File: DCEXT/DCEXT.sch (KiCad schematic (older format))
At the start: 5 parts, among them U1 MPCIE-Socket

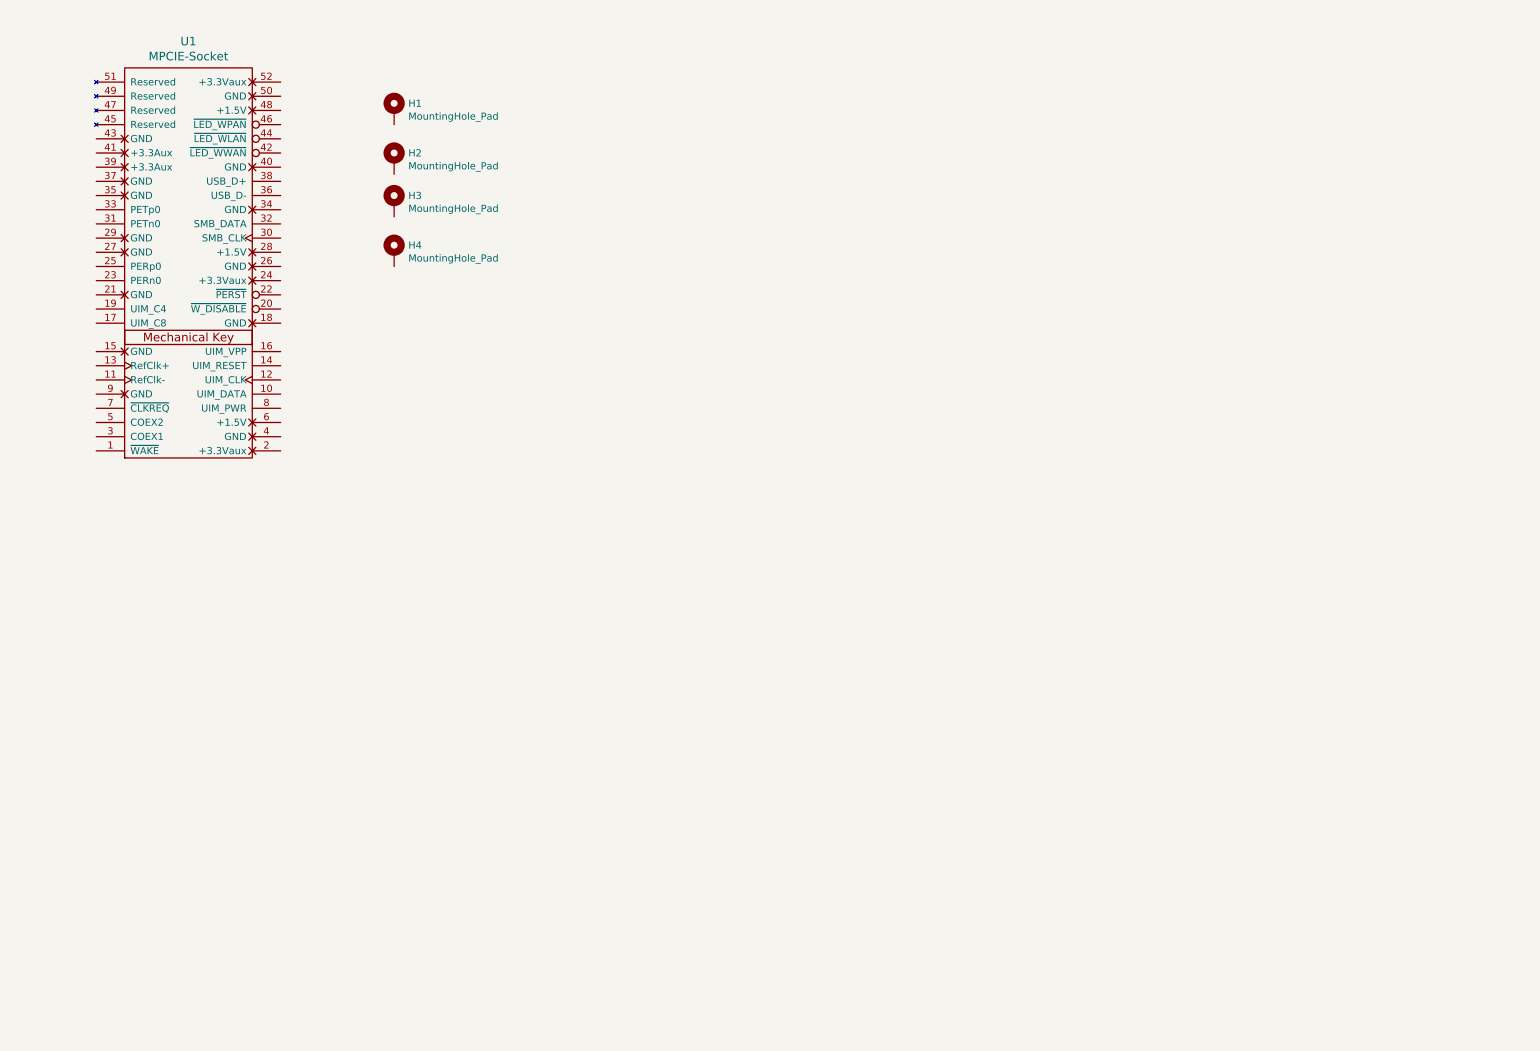
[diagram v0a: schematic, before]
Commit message: Add usb host connector and add more documentation
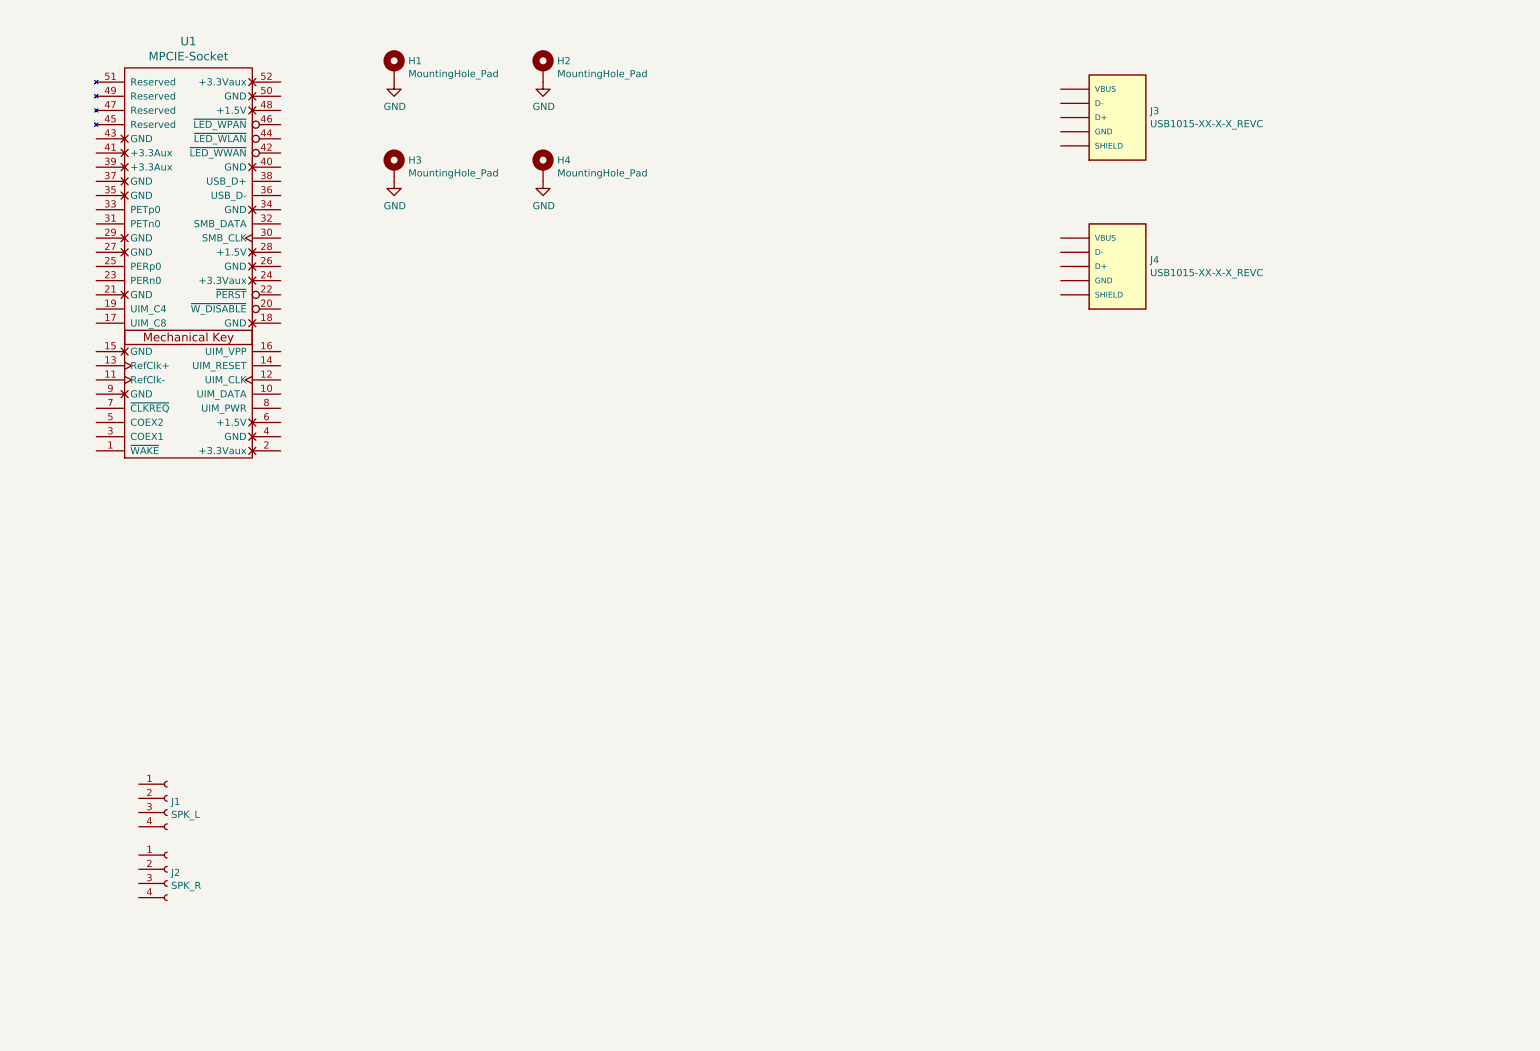
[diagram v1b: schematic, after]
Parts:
- added J1: SPK_L, symbol Connector:Conn_01x04_Female
- added J2: SPK_R, symbol Connector:Conn_01x04_Female
- added J3, J4: USB1015-XX-X-X_REVC, DCEXT:GCT_USB1015-XX-X-X_REVC, symbol USB1015-XX-X-X_REVC:USB1015-XX-X-X_REVC
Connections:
- net GND: now reaches H1.1
- net GND: now also H2.1, H3.1, H4.1
- new net: J3.5 (SHIELD), J3.6 (SHIELD), J3.7 (SHIELD), J3.8 (SHIELD)
- new net: J4.5 (SHIELD), J4.6 (SHIELD), J4.7 (SHIELD), J4.8 (SHIELD)
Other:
- moved on the sheet: H1, H2, H3, H4
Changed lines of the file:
@@
 L Mechanical:MountingHole_Pad H1
 U 1 1 613EA83B
-P 3200 1200
-F 0 "H1" H 3300 1249 50  0000 L CNN
-F 1 "MountingHole_Pad" H 3300 1158 50  0000 L CNN
-F 2 "MountingHole:MountingHole_5mm_Pad_TopBottom" H 3200 1200 50  0001 C CNN
-F 3 "~" H 3200 1200 50  0001 C CNN
-	1    3200 1200
+P 3200 900
+F 0 "H1" H 3300 949 50  0000 L CNN
+F 1 "MountingHole_Pad" H 3300 858 50  0000 L CNN
+F 2 "MountingHole:MountingHole_5mm_Pad_TopBottom" H 3200 900 50  0001 C CNN
+F 3 "~" H 3200 900 50  0001 C CNN
+	1    3200 900
 	1    0    0    -1
 $EndComp
@@
 L Mechanical:MountingHole_Pad H2
 U 1 1 613EB1E4
-P 3200 1550
-F 0 "H2" H 3300 1599 50  0000 L CNN
-F 1 "MountingHole_Pad" H 3300 1508 50  0000 L CNN
-F 2 "MountingHole:MountingHole_5mm_Pad_TopBottom" H 3200 1550 50  0001 C CNN
-F 3 "~" H 3200 1550 50  0001 C CNN
-	1    3200 1550
+P 4250 900
+F 0 "H2" H 4350 949 50  0000 L CNN
+F 1 "MountingHole_Pad" H 4350 858 50  0000 L CNN
+F 2 "MountingHole:MountingHole_5mm_Pad_TopBottom" H 4250 900 50  0001 C CNN
+F 3 "~" H 4250 900 50  0001 C CNN
+	1    4250 900
 	1    0    0    -1
 $EndComp
@@
 L Mechanical:MountingHole_Pad H3
 U 1 1 613EC01C
-P 3200 1850
-F 0 "H3" H 3300 1899 50  0000 L CNN
-F 1 "MountingHole_Pad" H 3300 1808 50  0000 L CNN
-F 2 "MountingHole:MountingHole_5mm_Pad_TopBottom" H 3200 1850 50  0001 C CNN
-F 3 "~" H 3200 1850 50  0001 C CNN
-	1    3200 1850
+P 3200 1600
+F 0 "H3" H 3300 1649 50  0000 L CNN
+F 1 "MountingHole_Pad" H 3300 1558 50  0000 L CNN
+F 2 "MountingHole:MountingHole_5mm_Pad_TopBottom" H 3200 1600 50  0001 C CNN
+F 3 "~" H 3200 1600 50  0001 C CNN
+	1    3200 1600
 	1    0    0    -1
 $EndComp
@@
 L Mechanical:MountingHole_Pad H4
 U 1 1 613EC022
-P 3200 2200
-F 0 "H4" H 3300 2249 50  0000 L CNN
-F 1 "MountingHole_Pad" H 3300 2158 50  0000 L CNN
-F 2 "MountingHole:MountingHole_5mm_Pad_TopBottom" H 3200 2200 50  0001 C CNN
-F 3 "~" H 3200 2200 50  0001 C CNN
-	1    3200 2200
+P 4250 1600
+F 0 "H4" H 4350 1649 50  0000 L CNN
+F 1 "MountingHole_Pad" H 4350 1558 50  0000 L CNN
+F 2 "MountingHole:MountingHole_5mm_Pad_TopBottom" H 4250 1600 50  0001 C CNN
+F 3 "~" H 4250 1600 50  0001 C CNN
+	1    4250 1600
 	1    0    0    -1
 $EndComp
+$Comp
+L power:GND #PWR0101
+U 1 1 613EFFE7
+P 3200 1000
+F 0 "#PWR0101" H 3200 750 50  0001 C CNN
+F 1 "GND" H 3205 827 50  0000 C CNN
+F 2 "" H 3200 1000 50  0001 C CNN
+F 3 "" H 3200 1000 50  0001 C CNN
+	1    3200 1000
+	1    0    0    -1
+$EndComp
+$Comp
+L power:GND #PWR0102
+U 1 1 613F3AAA
+P 4250 1000
+F 0 "#PWR0102" H 4250 750 50  0001 C CNN
+F 1 "GND" H 4255 827 50  0000 C CNN
+F 2 "" H 4250 1000 50  0001 C CNN
+F 3 "" H 4250 1000 50  0001 C CNN
+	1    4250 1000
+	1    0    0    -1
+$EndComp
+$Comp
+L power:GND #PWR0103
+U 1 1 613F73AE
+P 3200 1700
+F 0 "#PWR0103" H 3200 1450 50  0001 C CNN
+F 1 "GND" H 3205 1527 50  0000 C CNN
+F 2 "" H 3200 1700 50  0001 C CNN
+F 3 "" H 3200 1700 50  0001 C CNN
+	1    3200 1700
+	1    0    0    -1
+$EndComp
+$Comp
+L power:GND #PWR0104
+U 1 1 613F73B4
+P 4250 1700
+F 0 "#PWR0104" H 4250 1450 50  0001 C CNN
+F 1 "GND" H 4255 1527 50  0000 C CNN
+F 2 "" H 4250 1700 50  0001 C CNN
+F 3 "" H 4250 1700 50  0001 C CNN
+	1    4250 1700
+	1    0    0    -1
+$EndComp
+$Comp
+L Connector:Conn_01x04_Female J1
+U 1 1 613F78CA
+P 1600 6050
+F 0 "J1" H 1628 6026 50  0000 L CNN
+F 1 "SPK_L" H 1628 5935 50  0000 L CNN
+F 2 "" H 1600 6050 50  0001 C CNN
+F 3 "~" H 1600 6050 50  0001 C CNN
+	1    1600 6050
+	1    0    0    -1
+$EndComp
+$Comp
+L Connector:Conn_01x04_Female J2
+U 1 1 613F892F
+P 1600 6550
+F 0 "J2" H 1628 6526 50  0000 L CNN
+F 1 "SPK_R" H 1628 6435 50  0000 L CNN
+F 2 "" H 1600 6550 50  0001 C CNN
+F 3 "~" H 1600 6550 50  0001 C CNN
+	1    1600 6550
+	1    0    0    -1
+$EndComp
+$Comp
+L USB1015-XX-X-X_REVC:USB1015-XX-X-X_REVC J3
+U 1 1 613FFF39
+P 8300 1250
+F 0 "J3" H 8530 1296 50  0000 L CNN
+F 1 "USB1015-XX-X-X_REVC" H 8530 1205 50  0000 L CNN
+F 2 "DCEXT:GCT_USB1015-XX-X-X_REVC" H 8300 1250 50  0001 L BNN
+F 3 "" H 8300 1250 50  0001 L BNN
+F 4 "GCT" H 8300 1250 50  0001 L BNN "MANUFACTURER"
+	1    8300 1250
+	1    0    0    -1
+$EndComp
+$Comp
+L USB1015-XX-X-X_REVC:USB1015-XX-X-X_REVC J4
+U 1 1 61401222
+P 8300 2300
+F 0 "J4" H 8530 2346 50  0000 L CNN
+F 1 "USB1015-XX-X-X_REVC" H 8530 2255 50  0000 L CNN
+F 2 "DCEXT:GCT_USB1015-XX-X-X_REVC" H 8300 2300 50  0001 L BNN
+F 3 "" H 8300 2300 50  0001 L BNN
+F 4 "GCT" H 8300 2300 50  0001 L BNN "MANUFACTURER"
+	1    8300 2300
+	1    0    0    -1
+$EndComp

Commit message: Add usb protection, fan control and fpc connector for module
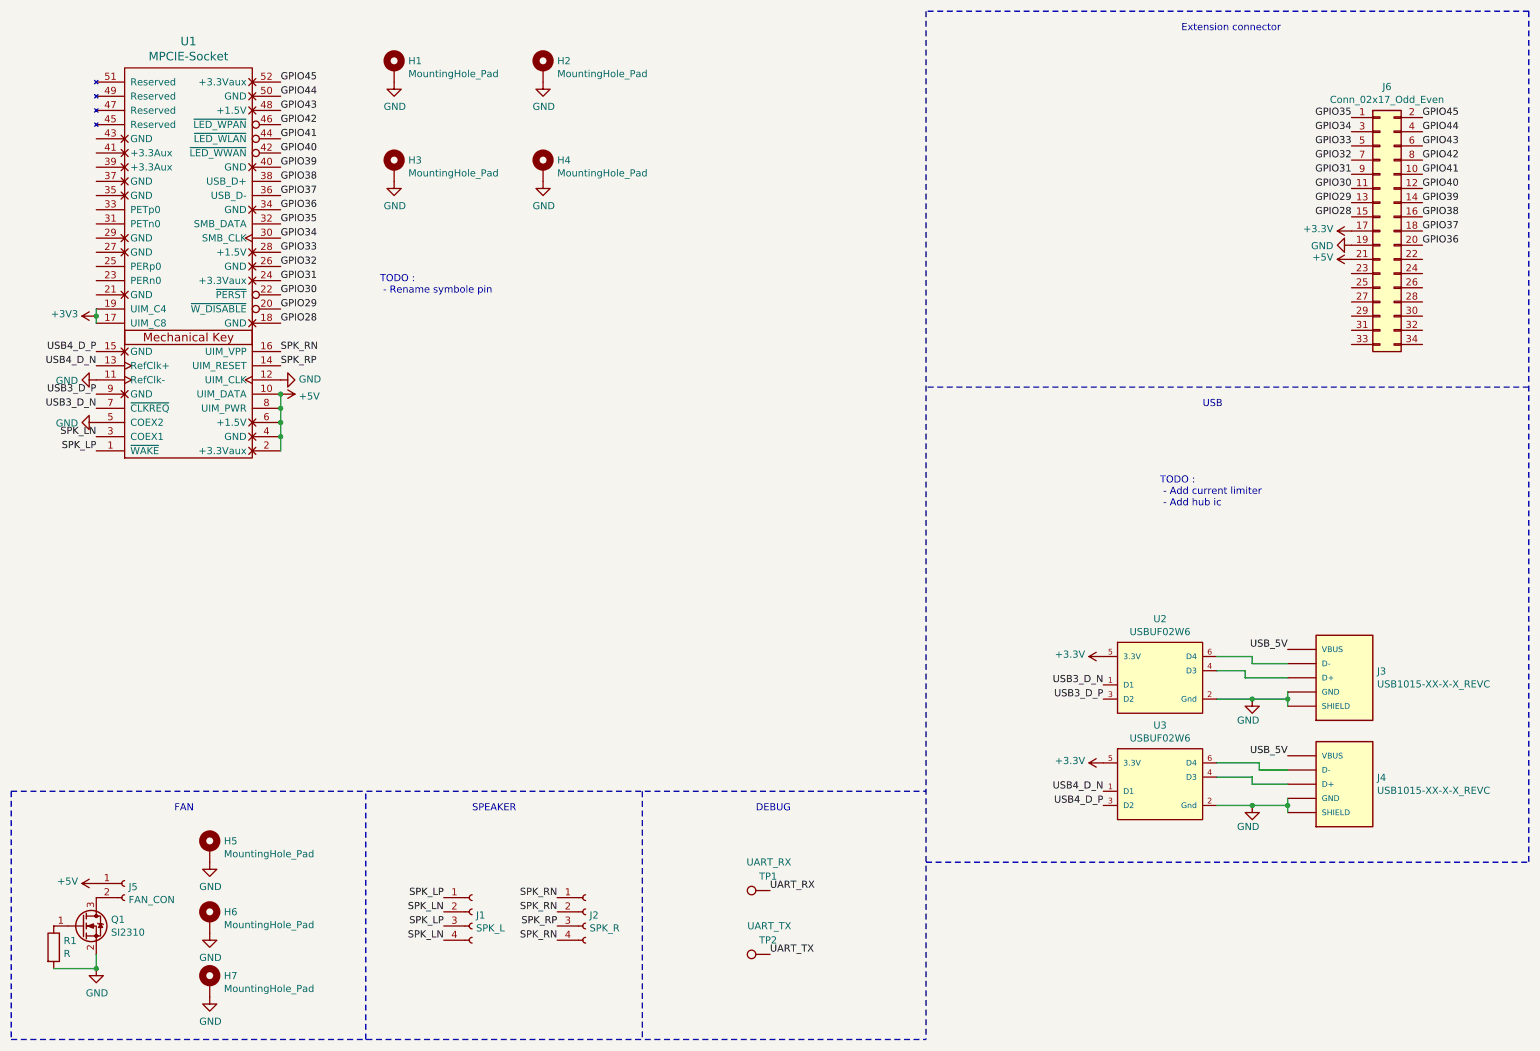
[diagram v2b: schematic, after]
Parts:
- added H5, H6, H7: MountingHole_Pad, MountingHole:MountingHole_2.2mm_M2_DIN965_Pad_TopBottom, symbol Mechanical:MountingHole_Pad
- added J5: FAN_CON, symbol Connector:Conn_01x02_Female
- added J6: Conn_02x17_Odd_Even, Connector_FFC-FPC:Hirose_FH12-34S-0.5SH_1x34-1MP_P0.50mm_Horizontal, symbol Connector_Generic:Conn_02x17_Odd_Even
- added Q1: SI2310, Package_TO_SOT_SMD:SOT-23, symbol Transistor_FET:2N7002
- added R1: R, Resistor_SMD:R_0402_1005Metric_Pad0.72x0.64mm_HandSolder, symbol Device:R
- added TP1: UART_RX, TestPoint:TestPoint_Pad_D2.5mm, symbol Connector:TestPoint
- added TP2: UART_TX, TestPoint:TestPoint_Pad_D2.5mm, symbol Connector:TestPoint
- added U2, U3: USBUF02W6, eec:ST_Microelectronics-USBUF02W6-0, symbol eec:USBUF02W6
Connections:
- net GND: now also J3.4 (GND), J3.5 (SHIELD), J3.6 (SHIELD), J3.7 (SHIELD), J3.8 (SHIELD), J4.4 (GND), J4.5 (SHIELD), J4.6 (SHIELD), J4.7 (SHIELD), J4.8 (SHIELD), U1.11 (RefClk-), U1.12 (UIM_CLK), U1.5 (COEX2), H5.1, H6.1, H7.1, J6.19 (Pin_19), Q1.2 (S), R1.2, U2.2 (Gnd), U3.2 (Gnd)
- net SPK_LP: now reaches U1.1 (~WAKE)
- net SPK_LP: now also J1.1 (Pin_1), J1.3 (Pin_3)
- net +5V: now reaches U1.10 (UIM_DATA)
- net +5V: now also U1.2 (+3.3Vaux), U1.4 (GND), U1.6 (+1.5V), U1.8 (UIM_PWR), J5.1 (Pin_1), J6.21 (Pin_21)
- net USB4_D_N: now reaches U1.13 (RefClk+)
- net USB4_D_N: now also U3.1 (D1)
- net SPK_RP: now reaches U1.14 (UIM_RESET)
- net SPK_RP: now also J2.3 (Pin_3)
- net USB4_D_P: now reaches U1.15 (GND)
- net USB4_D_P: now also U3.3 (D2)
- net SPK_RN: now reaches U1.16 (UIM_VPP)
- net SPK_RN: now also J2.1 (Pin_1), J2.2 (Pin_2), J2.4 (Pin_4)
- net +3V3: now reaches U1.17 (UIM_C8)
- net +3V3: now also U1.19 (UIM_C4), J6.17 (Pin_17), U2.5 (3.3V), U3.5 (3.3V)
- net GPIO28: now reaches U1.18 (GND)
- net GPIO28: now also J6.15 (Pin_15)
- net GPIO29: now reaches U1.20 (~W_DISABLE)
- net GPIO29: now also J6.13 (Pin_13)
- net GPIO30: now reaches U1.22 (~PERST)
- net GPIO30: now also J6.11 (Pin_11)
- net GPIO31: now reaches U1.24 (+3.3Vaux)
- net GPIO31: now also J6.9 (Pin_9)
- net GPIO32: now reaches U1.26 (GND)
- net GPIO32: now also J6.7 (Pin_7)
- net GPIO33: now reaches U1.28 (+1.5V)
- net GPIO33: now also J6.5 (Pin_5)
- net SPK_LN: now reaches U1.3 (COEX1)
- net SPK_LN: now also J1.2 (Pin_2), J1.4 (Pin_4)
- net GPIO34: now reaches U1.30 (SMB_CLK)
- net GPIO34: now also J6.3 (Pin_3)
- net GPIO35: now reaches U1.32 (SMB_DATA)
- net GPIO35: now also J6.1 (Pin_1)
- net GPIO36: now reaches U1.34 (GND)
- net GPIO36: now also J6.20 (Pin_20)
- net GPIO37: now reaches U1.36 (USB_D-)
- net GPIO37: now also J6.18 (Pin_18)
- net GPIO38: now reaches U1.38 (USB_D+)
- net GPIO38: now also J6.16 (Pin_16)
- net GPIO39: now reaches U1.40 (GND)
- net GPIO39: now also J6.14 (Pin_14)
- net GPIO40: now reaches U1.42 (~LED_WWAN)
- net GPIO40: now also J6.12 (Pin_12)
- net GPIO41: now reaches U1.44 (~LED_WLAN)
- net GPIO41: now also J6.10 (Pin_10)
- net GPIO42: now reaches U1.46 (~LED_WPAN)
- net GPIO42: now also J6.8 (Pin_8)
- net GPIO43: now reaches U1.48 (+1.5V)
- net GPIO43: now also J6.6 (Pin_6)
- net GPIO44: now reaches U1.50 (GND)
- net GPIO44: now also J6.4 (Pin_4)
- net GPIO45: now reaches U1.52 (+3.3Vaux)
- net GPIO45: now also J6.2 (Pin_2)
- net USB3_D_N: now reaches U1.7 (~CLKREQ)
- net USB3_D_N: now also U2.1 (D1)
- net USB3_D_P: now reaches U1.9 (GND)
- net USB3_D_P: now also U2.3 (D2)
- net USB_5V: now reaches J3.1 (VBUS)
- net USB_5V: now also J4.1 (VBUS)
- net at J3.2 (D-): now also U2.6 (D4)
- net at J3.3 (D+): now also U2.4 (D3)
- net at J4.2 (D-): now also U3.6 (D4)
- net at J4.3 (D+): now also U3.4 (D3)
- new net: Q1.1 (G), R1.1
- new net: J5.2 (Pin_2), Q1.3 (D)
- new net UART_RX: TP1.1
- new net UART_TX: TP2.1
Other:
- note added: "DEBUG"
- note added: "Extension connector"
- note added: "FAN"
- note added: "SPEAKER"
- note added: "TODO :\n - Add current limiter\n - Add hub ic"
- note added: "TODO :\n - Rename symbole pin"
- note added: "USB"
- moved on the sheet: J1, J2, J3, J4
